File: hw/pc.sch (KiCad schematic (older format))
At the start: 8 parts, among them U601 74HC191, U602 74HC191, U603 74HC191, U604 74HC191, U605 74HC10, U606 74HC00, U607 74HC541, U608 74HC541

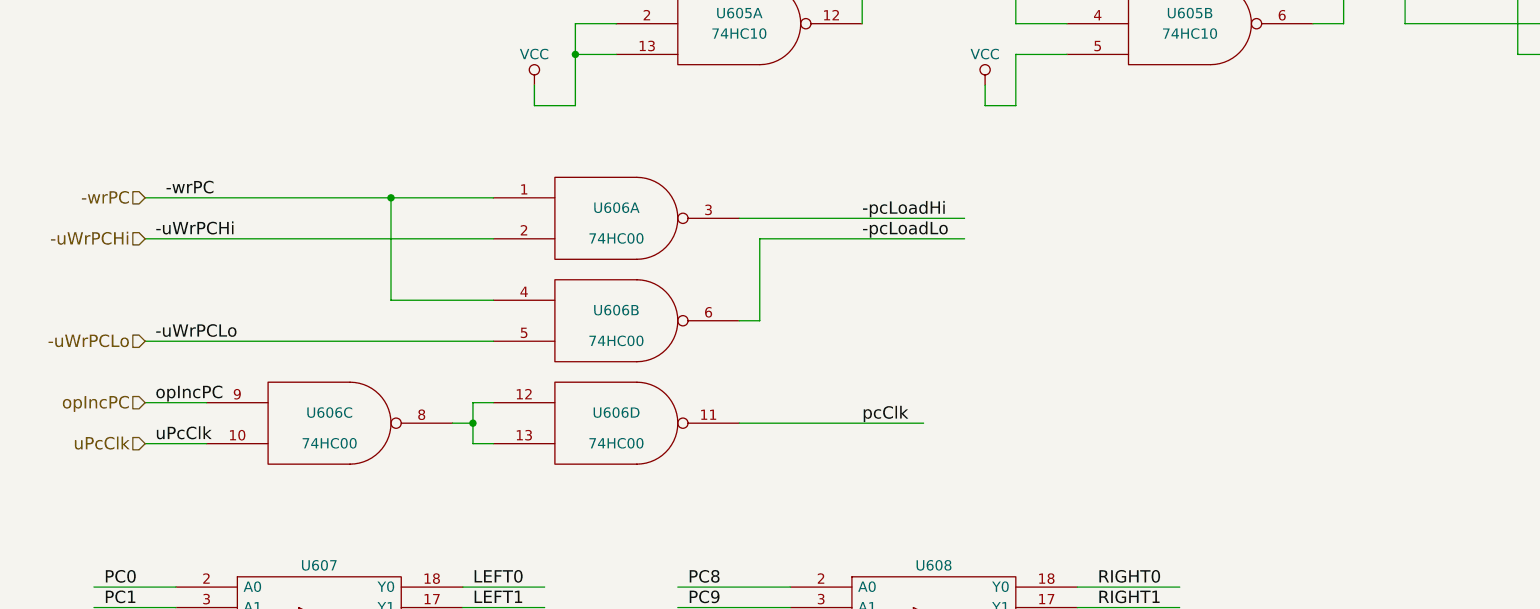
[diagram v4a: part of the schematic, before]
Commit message: fixed PC control logic
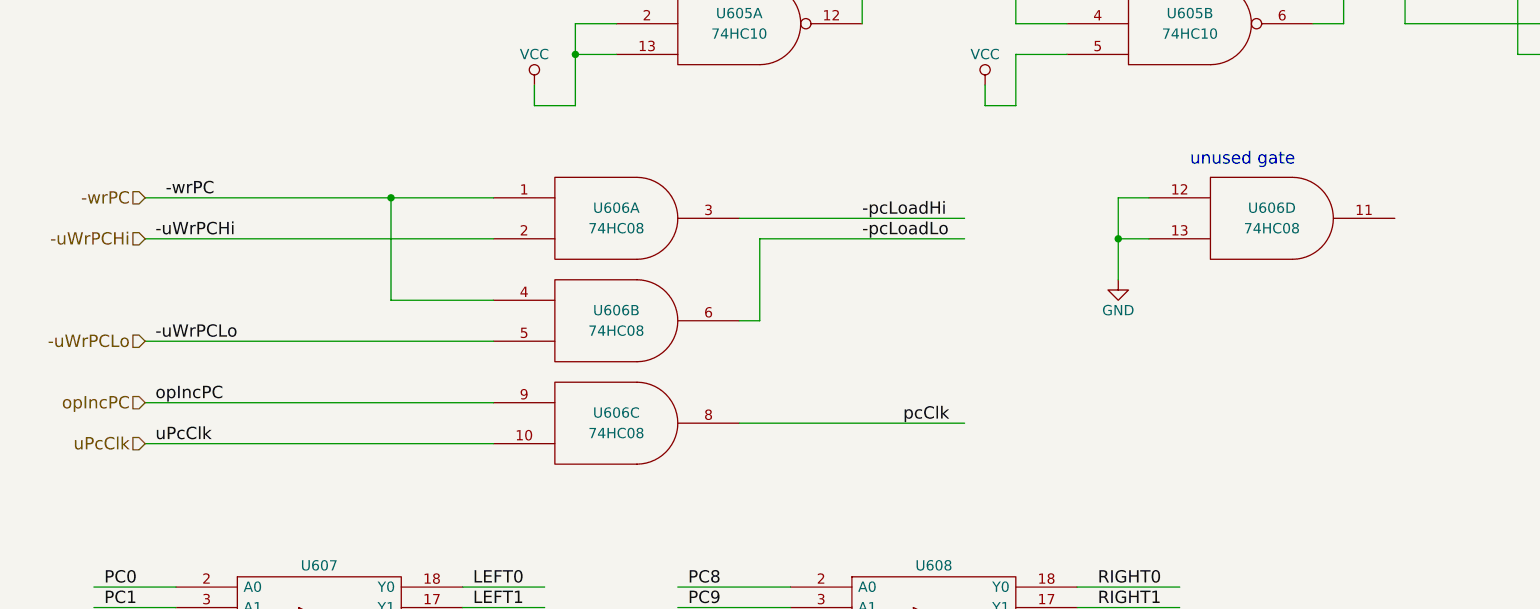
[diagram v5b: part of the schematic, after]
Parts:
- removed U606: 74HC00, symbol 74LS00
- added U606: 74HC08, symbol 74LS08
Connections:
- wire segments 187 -> 184
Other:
- note added: "unused gate"
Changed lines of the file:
@@
 	7700 3150 6450 3150
 Connection ~ 6450 3150
-$Comp
-L 74LS00 U606
-U 1 1 5940589C
-P 3850 4650
-F 0 "U606" H 3850 4700 50  0000 C CNN
-F 1 "74HC00" H 3850 4550 50  0000 C CNN
-F 2 "" H 3850 4650 50  0001 C CNN
-F 3 "" H 3850 4650 50  0001 C CNN
-	1    3850 4650
-	1    0    0    -1
-$EndComp
-$Comp
-L 74LS00 U606
-U 2 1 594058A3
-P 3850 5150
-F 0 "U606" H 3850 5200 50  0000 C CNN
-F 1 "74HC00" H 3850 5050 50  0000 C CNN
-F 2 "" H 3850 5150 50  0001 C CNN
-F 3 "" H 3850 5150 50  0001 C CNN
-	2    3850 5150
-	1    0    0    -1
-$EndComp
 Wire Wire Line
-	3250 4550 2750 4550
-Wire Wire Line
-	2750 4550 1550 4550
+	1550 4550 3250 4550
 Text Label 1650 4550 0    60   ~ 0
 -wrPC
@@
 Wire Wire Line
 	4550 4750 5550 4750
-$Comp
-L 74LS00 U606
-U 3 1 594058B4
-P 2450 5650
-F 0 "U606" H 2450 5700 50  0000 C CNN
-F 1 "74HC00" H 2450 5550 50  0000 C CNN
-F 2 "" H 2450 5650 50  0001 C CNN
-F 3 "" H 2450 5650 50  0001 C CNN
-	3    2450 5650
-	1    0    0    -1
-$EndComp
-$Comp
-L 74LS00 U606
-U 4 1 594058BB
-P 3850 5650
-F 0 "U606" H 3850 5700 50  0000 C CNN
-F 1 "74HC00" H 3850 5550 50  0000 C CNN
-F 2 "" H 3850 5650 50  0001 C CNN
-F 3 "" H 3850 5650 50  0001 C CNN
-	4    3850 5650
-	1    0    0    -1
-$EndComp
 Wire Wire Line
-	3250 5550 3150 5550
+	1550 5550 3250 5550
 Wire Wire Line
-	3150 5550 3150 5650
+	1550 5750 3250 5750
 Wire Wire Line
-	3150 5650 3150 5750
-Wire Wire Line
-	3150 5650 3050 5650
-Wire Wire Line
-	3150 5750 3250 5750
-Connection ~ 3150 5650
-Wire Wire Line
-	1850 5550 1550 5550
-Wire Wire Line
-	1850 5750 1550 5750
-Wire Wire Line
-	4450 5650 5350 5650
+	4450 5650 5550 5650
 Text Label 1600 5550 0    60   ~ 0
 opIncPC
@@
 Text Label 1400 1500 0    60   ~ 0
 pcClk
-Text Label 5050 5650 0    60   ~ 0
+Text Label 5250 5650 0    60   ~ 0
 pcClk
 Text HLabel 1550 5550 0    60   Input ~ 0
@@
 Text HLabel 1550 5750 0    60   Input ~ 0
 uPcClk
+$Comp
+L 74LS08 U606
+U 1 1 5943D28D
+P 3850 4650
+F 0 "U606" H 3850 4700 50  0000 C CNN
+F 1 "74HC08" H 3850 4600 50  0000 C CNN
+F 2 "" H 3850 4650 50  0001 C CNN
+F 3 "" H 3850 4650 50  0001 C CNN
+	1    3850 4650
+	1    0    0    -1
+$EndComp
+$Comp
+L 74LS08 U606
+U 2 1 5943D2BC
+P 3850 5150
+F 0 "U606" H 3850 5200 50  0000 C CNN
+F 1 "74HC08" H 3850 5100 50  0000 C CNN
+F 2 "" H 3850 5150 50  0001 C CNN
+F 3 "" H 3850 5150 50  0001 C CNN
+	2    3850 5150
+	1    0    0    -1
+$EndComp
+$Comp
+L 74LS08 U606
+U 3 1 5943D307
+P 3850 5650
+F 0 "U606" H 3850 5700 50  0000 C CNN
+F 1 "74HC08" H 3850 5600 50  0000 C CNN
+F 2 "" H 3850 5650 50  0001 C CNN
+F 3 "" H 3850 5650 50  0001 C CNN
+	3    3850 5650
+	1    0    0    -1
+$EndComp
+$Comp
+L 74LS08 U606
+U 4 1 5943D865
+P 7050 4650
+F 0 "U606" H 7050 4700 50  0000 C CNN
+F 1 "74HC08" H 7050 4600 50  0000 C CNN
+F 2 "" H 7050 4650 50  0001 C CNN
+F 3 "" H 7050 4650 50  0001 C CNN
+	4    7050 4650
+	1    0    0    -1
+$EndComp
+Wire Wire Line
+	6450 4550 6300 4550
+Wire Wire Line
+	6300 4550 6300 4950
+Wire Wire Line
+	6450 4750 6300 4750
+Connection ~ 6300 4750
+$Comp
+L GND #PWR?
+U 1 1 5943DB03
+P 6300 4950
+F 0 "#PWR?" H 6300 4700 50  0001 C CNN
+F 1 "GND" H 6300 4800 50  0000 C CNN
+F 2 "" H 6300 4950 50  0001 C CNN
+F 3 "" H 6300 4950 50  0001 C CNN
+	1    6300 4950
+	1    0    0    -1
+$EndComp
+Text Notes 6650 4400 0    60   ~ 0
+unused gate
 $EndSCHEMATC
